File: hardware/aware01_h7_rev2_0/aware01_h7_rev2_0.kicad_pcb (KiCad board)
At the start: 4 copper layers, 46 x 110 mm, 156 parts, among them IC1 587-2054-127F, IC2 587-2054-127F, IC3 587-2054-127F, IC4 587-2054-127F, IC5 TLV320AIC3204IRHBR, J1 Conn_02x07_Odd_Even, J10 GATE4_IN, J11 CV2_IN, J12 CV3_IN, J13 V/OCT_IN, J14 CV1_IN, J2 Conn_02x05_Odd_Even, J3 InL, J4 InR, J5 OutL, J6 OutR, J7 GATE1_IN, J8 GATE2_IN, J9 GATE3_IN, Q1 MMBT3904, Q2 MMBT3904, Q3 MMBT3904, Q4 MMBT3904, SW1 SW_Push, SW2 SW_Push, U1 LMR50410Y5FQDBVRQ1, U10 NE5532DRG4, U11 NE5532DRG4, U12 OPA2322AIDR, U13 OPA2322AIDR, U2 LM1117MP-3.3, U3 74AHCT1G14DBVRG4, U4 STM32H7A3RITx, U5 LM4040DIM3X-10, U6 10k, U7 10k, U8 10k, U9 10k, Y1 WE-XTAL 24.0MHz 50ppm

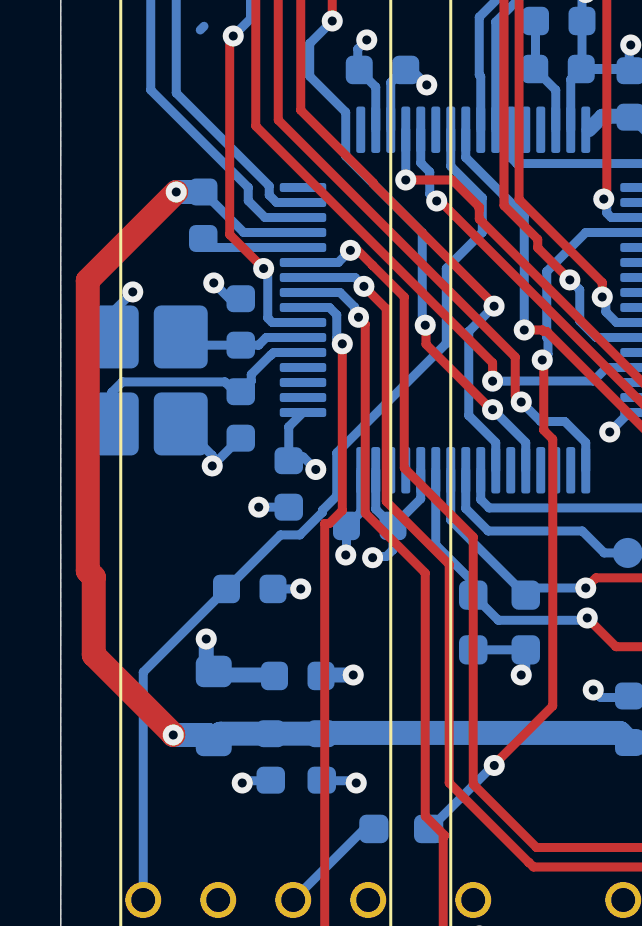
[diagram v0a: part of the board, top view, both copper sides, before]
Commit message: hardware: switch crystal and calculate load caps
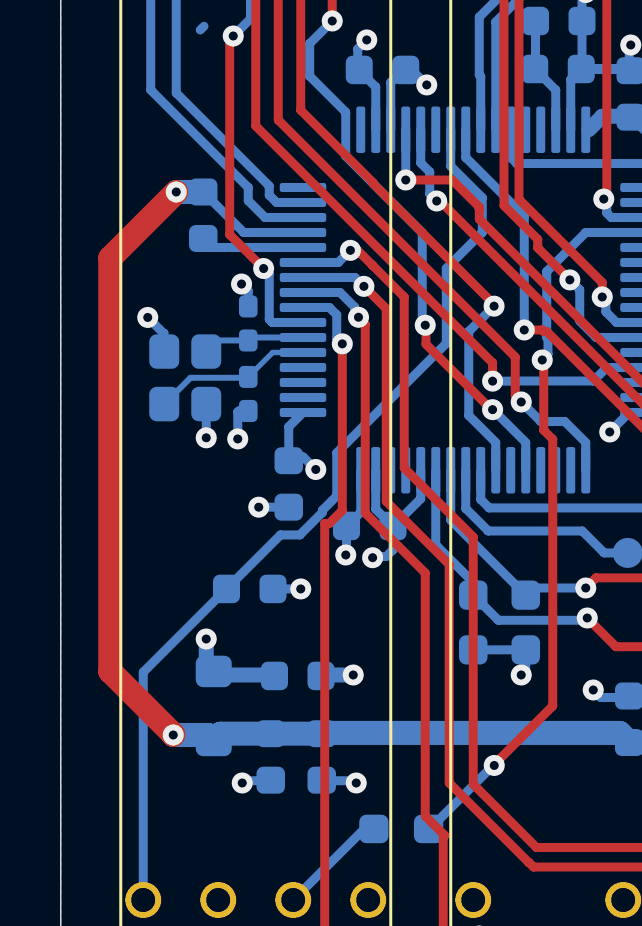
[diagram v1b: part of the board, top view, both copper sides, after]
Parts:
- C17, C21: value 22p -> 14pF; footprint Capacitor_SMD:C_0603_1608Metric -> Capacitor_SMD:C_0402_1005Metric_Pad0.74x0.62mm_HandSolder
- Y1: footprint Crystal:Crystal_SMD_3225-4Pin_3.2x2.5mm_HandSoldering -> Crystal:Crystal_SMD_2520-4Pin_2.5x2.0mm
- moved Y1 1.30 mm to (134.3, 86.5)
- moved C17 0.74 mm to (136.4, 87.0)
- moved C21 0.25 mm to (136.4, 84.7)
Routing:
- net Net-(U4-PH0): track 8.46 -> 5.37 mm
- net GND: track 132.9 -> 131.0 mm, vias 99 -> 100
- net Net-(U4-PH1): track 4.30 -> 3.42 mm
- net +3.3VA: track 46.9 -> 46.3 mm

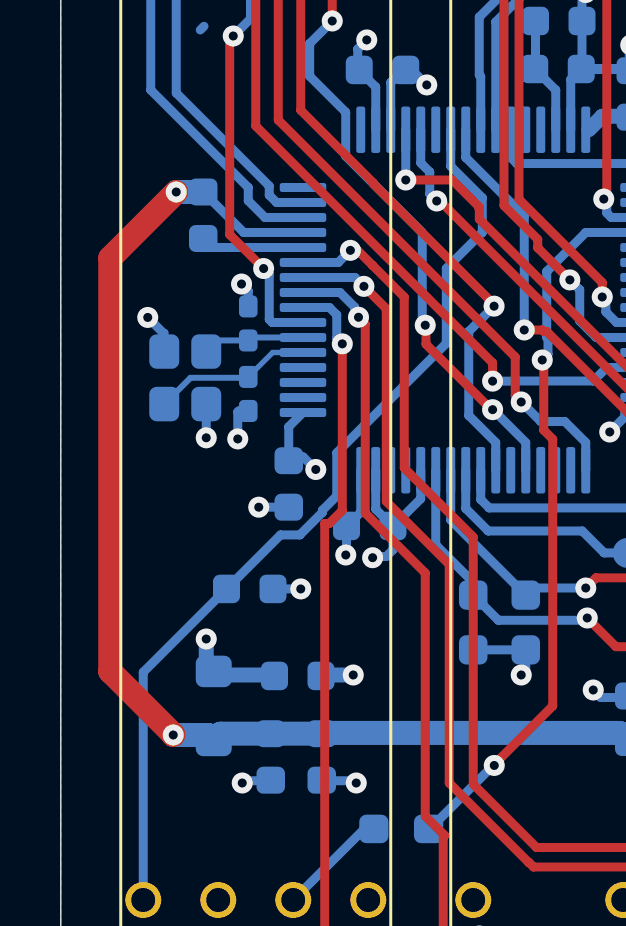
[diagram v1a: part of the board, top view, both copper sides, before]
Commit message: hardware: add GND shielding around crystal
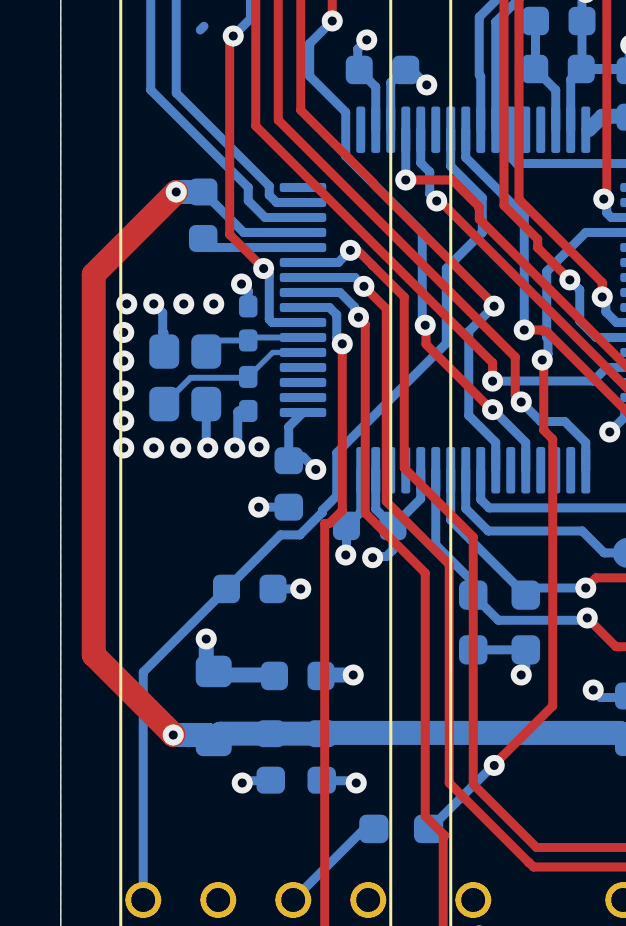
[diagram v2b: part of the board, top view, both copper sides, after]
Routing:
- net GND: track 131.0 -> 132.1 mm, vias 100 -> 111
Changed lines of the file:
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@@
 		(descr "SMD2520/4, Crystal, 2.5x2.0mm package, SMD, generated with kicad-footprint-generator make_crystal.py, http://www.newxtal.com/UploadFiles/Images/2012-11-12-09-29-09-776.pdf")
 		(property "Reference" "Y1"
-			(at -2.6875 -1.2 0)
+			(at -0.2375 -2.85 0)
 			(layer "B.SilkS")
 			(effects
@@
 		(tags "capacitor handsolder")
 		(property "Reference" "C21"
-			(at 0.65 -1.9 0)
+			(at 0.65 -1.75 0)
 			(layer "B.SilkS")
 			(effects
@@
 	)
 	(via
-		(at 135.05 88.4625)
+		(at 135.1 88.8)
 		(size 0.7)
 		(drill 0.3)
@@
 	)
 	(via
+		(at 134.3 84)
+		(size 0.7)
+		(drill 0.3)
+		(layers "F.Cu" "B.Cu")
+		(free yes)
+		(net 1)
+	)
+	(via
 		(at 154.9 46.3)
 		(size 0.7)
@@
 	)
 	(via
+		(at 133.3 88.8)
+		(size 0.7)
+		(drill 0.3)
+		(layers "F.Cu" "B.Cu")
+		(free yes)
+		(net 1)
+	)
+	(via
+		(at 132.4 84)
+		(size 0.7)
+		(drill 0.3)
+		(layers "F.Cu" "B.Cu")
+		(free yes)
+		(net 1)
+	)
+	(via
 		(at 171.1 51.9)
 		(size 0.7)
@@
 	)
 	(via
-		(at 136.1 88.5)
+		(at 136 88.8)
 		(size 0.7)
 		(drill 0.3)
@@
 	)
 	(via
+		(at 132.3 87.9)
+		(size 0.7)
+		(drill 0.3)
+		(layers "F.Cu" "B.Cu")
+		(free yes)
+		(net 1)
+	)
+	(via
+		(at 135.3 84)
+		(size 0.7)
+		(drill 0.3)
+		(layers "F.Cu" "B.Cu")
+		(free yes)
+		(net 1)
+	)
+	(via
 		(at 166.9 90.3)
 		(size 0.7)
@@
 	)
 	(via
+		(at 134.2 88.8)
+		(size 0.7)
+		(drill 0.3)
+		(layers "F.Cu" "B.Cu")
+		(free yes)
+		(net 1)
+	)
+	(via
 		(at 170.7 49.3)
 		(size 0.7)
@@
 	)
 	(via
+		(at 132.3 86.9)
+		(size 0.7)
+		(drill 0.3)
+		(layers "F.Cu" "B.Cu")
+		(free yes)
+		(net 1)
+	)
+	(via
 		(at 170.7 47.3)
 		(size 0.7)
@@
 	)
 	(via
+		(at 132.3 85.9)
+		(size 0.7)
+		(drill 0.3)
+		(layers "F.Cu" "B.Cu")
+		(free yes)
+		(net 1)
+	)
+	(via
 		(at 138.2 93.5)
 		(size 0.7)
@@
 	)
 	(via
-		(at 133.1 84.45)
+		(at 132.3 84.95)
+		(size 0.7)
+		(drill 0.3)
+		(layers "F.Cu" "B.Cu")
+		(free yes)
+		(net 1)
+	)
+	(via
+		(at 133.3 84)
 		(size 0.7)
 		(drill 0.3)
@@
 	)
 	(via
+		(at 132.3 88.8)
+		(size 0.7)
+		(drill 0.3)
+		(layers "F.Cu" "B.Cu")
+		(free yes)
+		(net 1)
+	)
+	(via
 		(at 142.85 116.56875)
 		(size 0.7)
@@
 	)
 	(via
+		(at 136.808678 88.763009)
+		(size 0.7)
+		(drill 0.3)
+		(layers "F.Cu" "B.Cu")
+		(free yes)
+		(net 1)
+	)
+	(via
 		(at 160.775 91.93375)
 		(size 0.7)
@@
 	)
 	(segment
+		(start 135.05 87.3375)
+		(end 135.05 88.75)
+		(width 0.3)
+		(layer "B.Cu")
+		(net 1)
+	)
+	(segment
 		(start 168.7 96.36875)
 		(end 168.925 96.59375)
@@
 	)
 	(segment
+		(start 136.1 88.7)
+		(end 136.1 87.6)
+		(width 0.3)
+		(layer "B.Cu")
+		(net 1)
+	)
+	(segment
 		(start 136.3 146.6125)
 		(end 136.3 146.7)
@@
 	)
 	(segment
-		(start 136.1 87.6)
-		(end 136.1325 87.5675)
-		(width 0.3)
-		(layer "B.Cu")
-		(net 1)
-	)
-	(segment
 		(start 150.875 76.16875)
 		(end 151.45 75.59375)
@@
 	)
 	(segment
-		(start 136.1325 87.5675)
-		(end 136.45 87.5675)
-		(width 0.3)
-		(layer "B.Cu")
-		(net 1)
-	)
-	(segment
 		(start 167.2 142.1)
 		(end 166.861 142.439)
@@
 	)
 	(segment
+		(start 136.1325 87.5675)
+		(end 136.45 87.5675)
+		(width 0.3)
+		(layer "B.Cu")
+		(net 1)
+	)
+	(segment
+		(start 136.1 87.6)
+		(end 136.1325 87.5675)
+		(width 0.3)
+		(layer "B.Cu")
+		(net 1)
+	)
+	(segment
 		(start 147.575 76.14375)
 		(end 147.55 76.16875)
@@
 	)
 	(segment
-		(start 136.1 88.5)
-		(end 136.1 87.6)
-		(width 0.3)
-		(layer "B.Cu")
-		(net 1)
-	)
-	(segment
 		(start 149.95 117.69375)
 		(end 149.325 117.69375)
@@
 	)
 	(segment
+		(start 133.6 84.95)
+		(end 133.625 84.975)
+		(width 0.3)
+		(layer "B.Cu")
+		(net 1)
+	)
+	(segment
 		(start 170.3 127.8)
 		(end 170.1 127.6)
@@
 	)
 	(segment
+		(start 136 88.8)
+		(end 136.1 88.7)
+		(width 0.3)
+		(layer "B.Cu")
+		(net 1)
+	)
+	(segment
 		(start 148.2 97.11875)
 		(end 147.95 96.86875)
@@
 	)
 	(segment
+		(start 133.625 84.975)
+		(end 133.65 84.975)
+		(width 0.3)
+		(layer "B.Cu")
+		(net 1)
+	)
+	(segment
+		(start 133.3 84)
+		(end 133.6 84.3)
+		(width 0.3)
+		(layer "B.Cu")
+		(net 1)
+	)
+	(segment
 		(start 173.7 92.5875)
 		(end 173.7 91.3)
@@
 	)
 	(segment
-		(start 153.760942 96.631093)
-		(end 153.900228 96.631093)
+		(start 135.05 88.75)
+		(end 135.1 88.8)
 		(width 0.3)
 		(layer "B.Cu")
@@
 	)
 	(segment
-		(start 168.725 99.43125)
-		(end 168.725 97.56875)
+		(start 153.760942 96.631093)
+		(end 153.900228 96.631093)
 		(width 0.3)
 		(layer "B.Cu")
@@
 	)
 	(segment
-		(start 133.625 84.975)
-		(end 133.65 84.975)
+		(start 168.725 99.43125)
+		(end 168.725 97.56875)
 		(width 0.3)
 		(layer "B.Cu")
@@
 	)
 	(segment
-		(start 135.05 87.3375)
-		(end 135.05 88.4625)
-		(width 0.3)
-		(layer "B.Cu")
-		(net 1)
-	)
-	(segment
-		(start 133.1 84.45)
-		(end 133.625 84.975)
-		(width 0.3)
-		(layer "B.Cu")
-		(net 1)
-	)
-	(segment
 		(start 142.2 90.49375)
 		(end 141.275 91.41875)
@@
 	)
 	(segment
+		(start 133.6 84.3)
+		(end 133.6 84.95)
+		(width 0.3)
+		(layer "B.Cu")
+		(net 1)
+	)
+	(segment
 		(start 137.325 52.49375)
 		(end 137.2 52.61875)
@@
 	)
 	(segment
-		(start 131.85 82.46875)
-		(end 134.05 80.26875)
+		(start 133.95 98.35)
+		(end 131.3 95.7)
 		(width 0.8)
 		(layer "F.Cu")
@@
 	)
 	(segment
-		(start 133.95 98.36875)
-		(end 133.95 98.35)
+		(start 131.3 83.01875)
+		(end 134.05 80.26875)
 		(width 0.8)
 		(layer "F.Cu")
@@
 	)
 	(segment
-		(start 131.85 96.25)
-		(end 131.85 82.46875)
+		(start 133.95 98.36875)
+		(end 133.95 98.35)
 		(width 0.8)
 		(layer "F.Cu")
@@
 	)
 	(segment
-		(start 133.95 98.35)
-		(end 131.85 96.25)
+		(start 131.3 95.7)
+		(end 131.3 83.01875)
 		(width 0.8)
 		(layer "F.Cu")

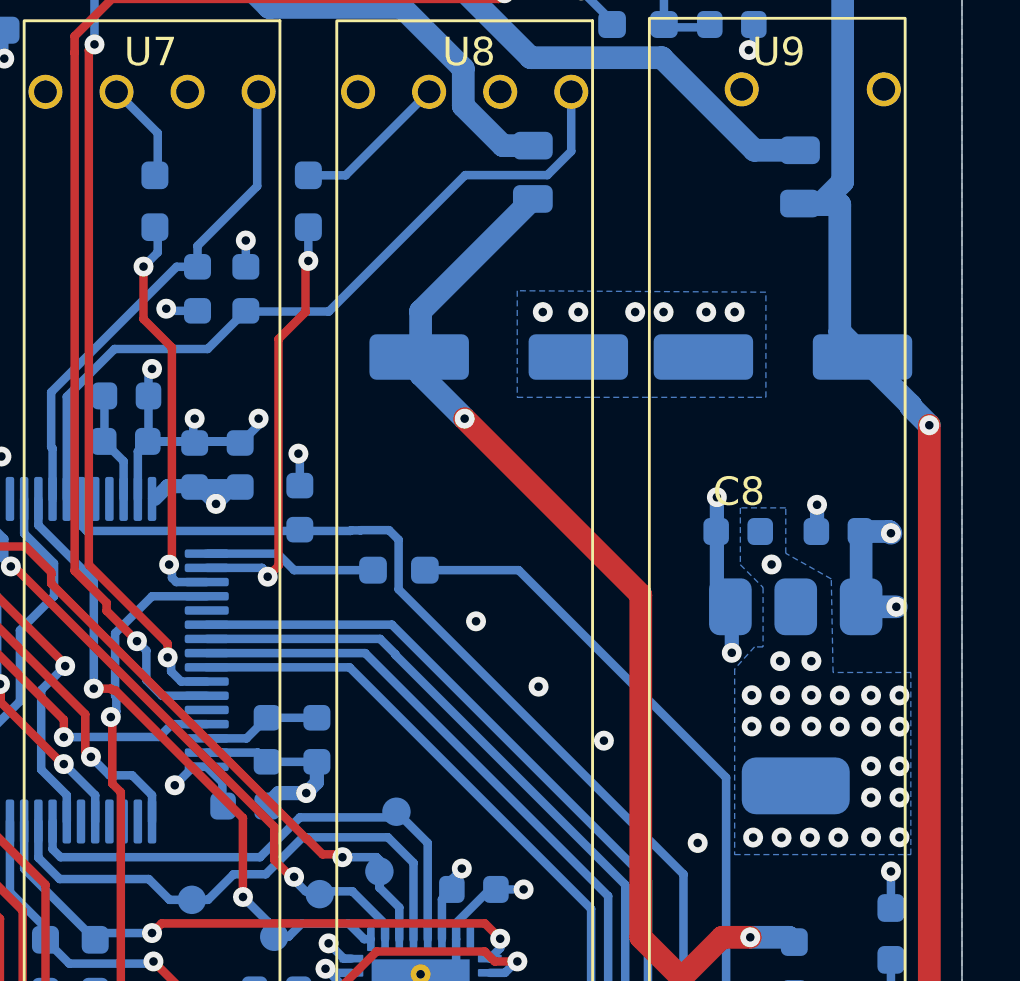
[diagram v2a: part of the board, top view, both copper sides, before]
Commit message: hw: improve design after design review (WIP)
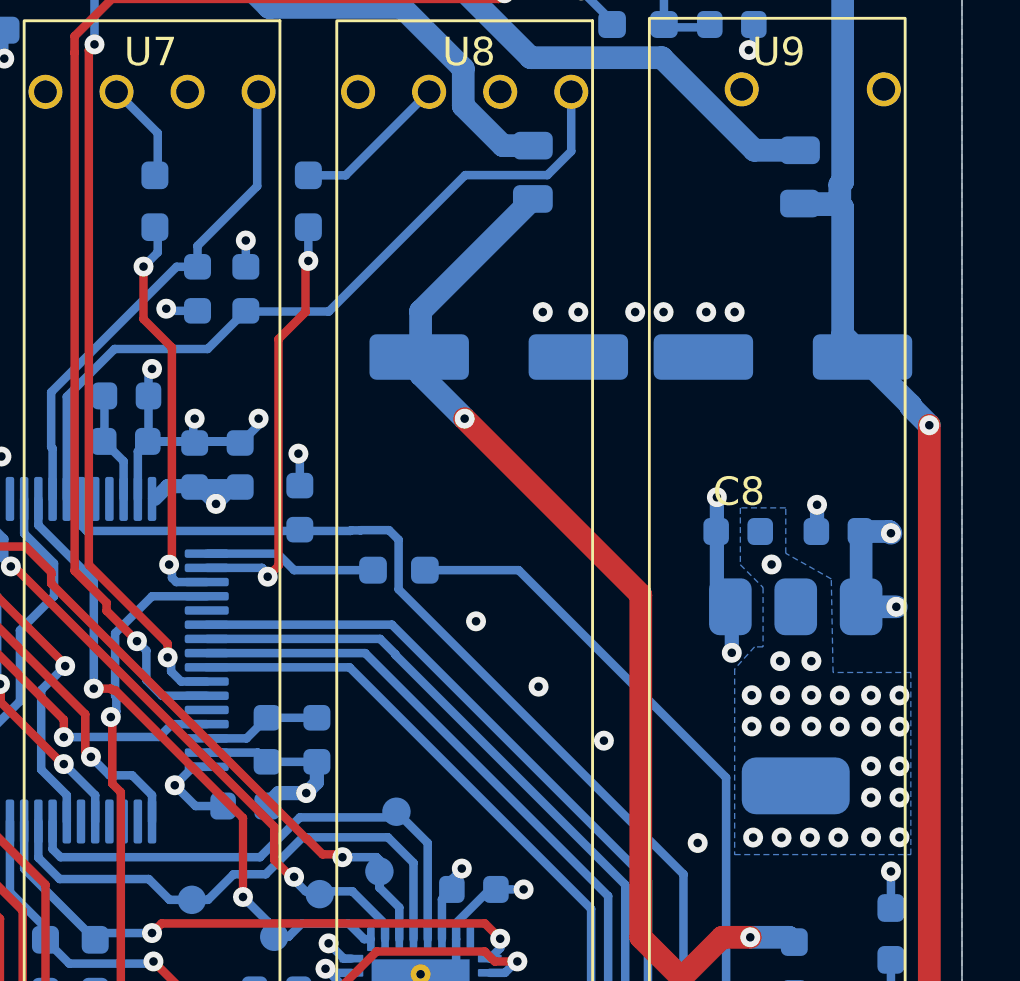
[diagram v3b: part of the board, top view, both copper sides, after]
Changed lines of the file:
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@@
 	)
 	(segment
-		(start 170.5375 67.8375)
-		(end 170.5 67.8)
+		(start 167.099 54.299)
+		(end 167.099 50.7885)
 		(width 0.8)
 		(layer "B.Cu")
@@
 	)
 	(segment
-		(start 166.951 50.7885)
-		(end 167.099 50.7885)
+		(start 170.5375 67.8375)
+		(end 170.5 67.8)
 		(width 0.8)
 		(layer "B.Cu")
@@
 	)
 	(segment
-		(start 171.237499 67.8)
-		(end 172 67.037499)
+		(start 166.951 50.7885)
+		(end 167.099 50.7885)
 		(width 0.8)
 		(layer "B.Cu")
@@
 	)
 	(segment
-		(start 174.4 74.9)
-		(end 172.7 73.2)
+		(start 172 72.41875)
+		(end 172 67.9375)
 		(width 0.8)
 		(layer "B.Cu")
@@
 	)
 	(segment
-		(start 172 59.2)
-		(end 167.099 54.299)
+		(start 172.75 73.16875)
+		(end 172 72.41875)
 		(width 0.8)
 		(layer "B.Cu")
@@
 	)
 	(segment
-		(start 172 67.037499)
-		(end 172 59.2)
+		(start 174.4 74.9)
+		(end 172.7 73.2)
 		(width 0.8)
 		(layer "B.Cu")
@@
 	)
 	(segment
+		(start 172 59.2)
+		(end 167.099 54.299)
+		(width 0.8)
+		(layer "B.Cu")
+		(net 2)
+	)
+	(segment
 		(start 169.025 50.7)
 		(end 169.2 50.875)
@@
 	)
 	(segment
-		(start 172.75 73.16875)
-		(end 171.9 72.31875)
+		(start 172 67.037499)
+		(end 172 59.2)
 		(width 0.8)
 		(layer "B.Cu")
@@
 	)
 	(segment
+		(start 171.9 67.137499)
+		(end 172 67.037499)
+		(width 0.8)
+		(layer "B.Cu")
+		(net 2)
+	)
+	(segment
 		(start 145.575 147.66875)
 		(end 145.05 148.19375)
@@
 	)
 	(segment
-		(start 167.099 54.299)
-		(end 167.099 50.7885)
+		(start 172 67.9375)
+		(end 171.9 67.8375)
 		(width 0.8)
 		(layer "B.Cu")
@@
 	)
 	(segment
-		(start 170.5 67.8)
-		(end 171.237499 67.8)
+		(start 171.9 67.8375)
+		(end 171.9 67.137499)
+		(width 0.8)
+		(layer "B.Cu")
+		(net 2)
+	)
+	(segment
+		(start 171.8625 67.8)
+		(end 171.9 67.8375)
 		(width 0.8)
 		(layer "B.Cu")
@@
 	)
 	(segment
+		(start 170.5 67.8)
+		(end 171.8625 67.8)
+		(width 0.8)
+		(layer "B.Cu")
+		(net 2)
+	)
+	(segment
 		(start 174.4 74.95)
 		(end 174.4 74.9)
@@
 	)
 	(segment
-		(start 171.9 72.31875)
-		(end 171.9 67.8375)
-		(width 0.8)
-		(layer "B.Cu")
-		(net 2)
-	)
-	(segment
 		(start 166.55 50.7)
 		(end 166.8625 50.7)
@@
 	)
 	(segment
-		(start 150.175 88.16875)
-		(end 150.175 88.96875)
-		(width 0.3)
-		(layer "B.Cu")
-		(net 3)
-	)
-	(segment
 		(start 157.9 93.68375)
 		(end 157.9 92.28375)
@@
 	)
 	(segment
+		(start 149.23125 89)
+		(end 148.5 88.26875)
+		(width 0.3)
+		(layer "B.Cu")
+		(net 3)
+	)
+	(segment
 		(start 137.575 61.7)
 		(end 137.3 61.7)
@@
 	)
 	(segment
+		(start 150.2 89)
+		(end 149.23125 89)
+		(width 0.3)
+		(layer "B.Cu")
+		(net 3)
+	)
+	(segment
 		(start 173.7 98.01875)
 		(end 173.7 99.11875)
@@
 	)
 	(segment
-		(start 149.625 87.61875)
-		(end 150.175 88.16875)
-		(width 0.3)
-		(layer "B.Cu")
-		(net 3)
-	)
-	(segment
 		(start 141.86875 76.16875)
 		(end 141.65 76.16875)
@@
 	)
 	(zone
-		(net 1)
-		(net_name "GND")
-		(layer "B.Cu")
-		(hatch edge 0.5)
-		(priority 2)
-		(connect_pads
-			(clearance 0.5)
-		)
-		(min_thickness 0.25)
-		(filled_areas_thickness no)
-		(fill yes
-			(thermal_gap 0.5)
-			(thermal_bridge_width 0.5)
-		)
-		(polygon
-			(pts
-				(xy 169.3 70.91875) (xy 160.55 70.86875) (xy 160.55 74.61875) (xy 168.95 74.61875) (xy 169.3 74.61875)
-			)
-		)
-	)
-	(zone
